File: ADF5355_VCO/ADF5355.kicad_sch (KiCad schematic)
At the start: 16 parts

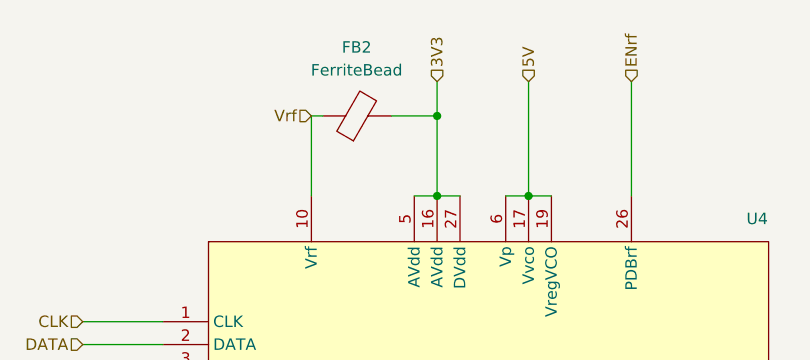
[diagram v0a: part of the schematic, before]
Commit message: Changed the power port
Changed all power ports to be global instead of them being hierarchical sheet pins
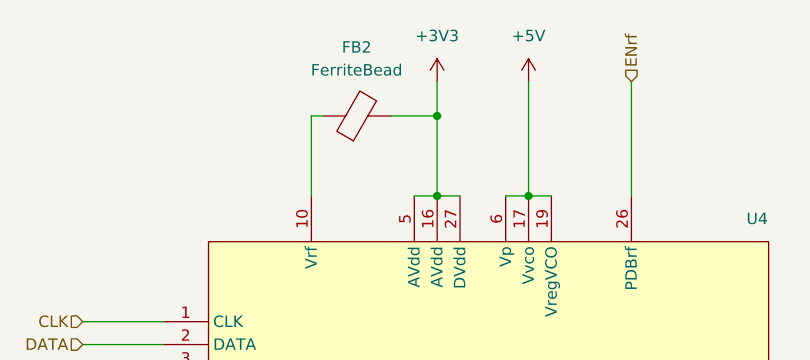
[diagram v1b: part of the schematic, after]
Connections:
- net Vrf: no longer FB2.1, U4.10 (Vrf)
- net 3V3 renamed +3V3
- net 5V renamed +5V
- new net: FB2.1, U4.10 (Vrf)
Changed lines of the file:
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@@
-    (effects (font (size 1.27 1.27)) (justify left))
-  )
-  (hierarchical_label "5V" (shape input) (at 146.05 43.18 90) (fields_autoplaced)
     (effects (font (size 1.27 1.27)) (justify left))
   )
@@
     (effects (font (size 1.27 1.27)) (justify right))
   )
-  (hierarchical_label "Vrf" (shape input) (at 121.92 46.99 180) (fields_autoplaced)
-    (effects (font (size 1.27 1.27)) (justify right))
-  )
   (hierarchical_label "Vrf" (shape input) (at 185.42 66.04 90) (fields_autoplaced)
     (effects (font (size 1.27 1.27)) (justify left))
@@
   )
   (hierarchical_label "RFoutB" (shape input) (at 203.2 100.33 0) (fields_autoplaced)
-    (effects (font (size 1.27 1.27)) (justify left))
-  )
-  (hierarchical_label "3V3" (shape input) (at 135.89 43.18 90) (fields_autoplaced)
     (effects (font (size 1.27 1.27)) (justify left))
   )
@@
     )
   )
+  (symbol (lib_id "power:+5V") (at 146.05 43.18 0) (unit 1)
+    (in_bom yes) (on_board yes) (dnp no) (fields_autoplaced)
+    (property "Reference" "#PWR043" (at 146.05 46.99 0)
+      (effects (font (size 1.27 1.27)) hide)
+    )
+    (property "Value" "+5V" (at 146.05 38.1 0)
+      (effects (font (size 1.27 1.27)))
+    )
+    (property "Footprint" "" (at 146.05 43.18 0)
+      (effects (font (size 1.27 1.27)) hide)
+    )
+    (property "Datasheet" "" (at 146.05 43.18 0)
+      (effects (font (size 1.27 1.27)) hide)
+    )
+    (pin "1")
+    (instances
+      (project "ADF5355_VCO"
+        (path "/29349b68-071c-451b-9b1e-10b5ef7e12a6/ea810e70-e3dc-4641-ad7c-8ecf7484ded2"
+          (reference "#PWR043") (unit 1)
+        )
+      )
+    )
+  )
   (symbol (lib_id "Device:R") (at 215.9 81.28 90) (unit 1)
     (in_bom yes) (on_board yes) (dnp no)
@@
         )
       )
+    )
+  )
+  (symbol (lib_id "power:+3V3") (at 135.89 43.18 0) (unit 1)
+    (in_bom yes) (on_board yes) (dnp no) (fields_autoplaced)
+    (property "Reference" "#PWR042" (at 135.89 46.99 0)
+      (effects (font (size 1.27 1.27)) hide)
+    )
+    (property "Value" "+3V3" (at 135.89 38.1 0)
+      (effects (font (size 1.27 1.27)))
+    )
+    (property "Footprint" "" (at 135.89 43.18 0)
+      (effects (font (size 1.27 1.27)) hide)
+    )
+    (property "Datasheet" "" (at 135.89 43.18 0)
+      (effects (font (size 1.27 1.27)) hide)
+    )
+    (pin "1")
+    (instances
+      (project "ADF5355_VCO"
+        (path "/29349b68-071c-451b-9b1e-10b5ef7e12a6/ea810e70-e3dc-4641-ad7c-8ecf7484ded2"
+          (reference "#PWR042") (unit 1)
+        )
+      )

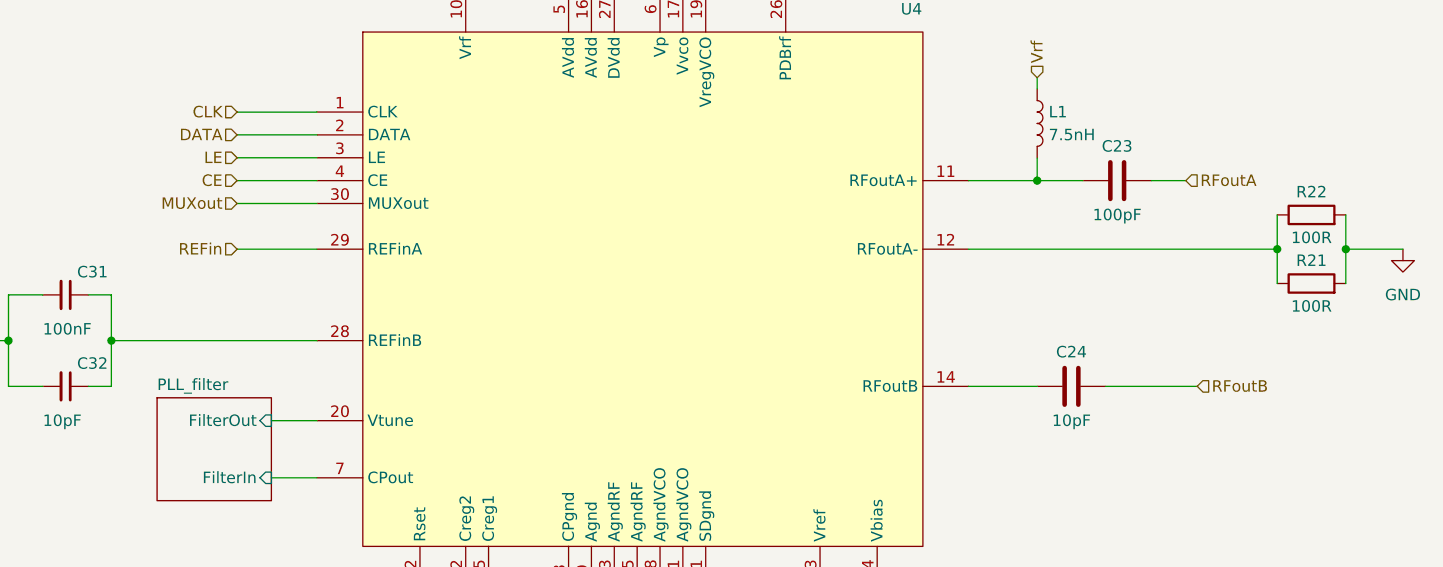
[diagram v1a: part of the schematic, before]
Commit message: Added RF connectors
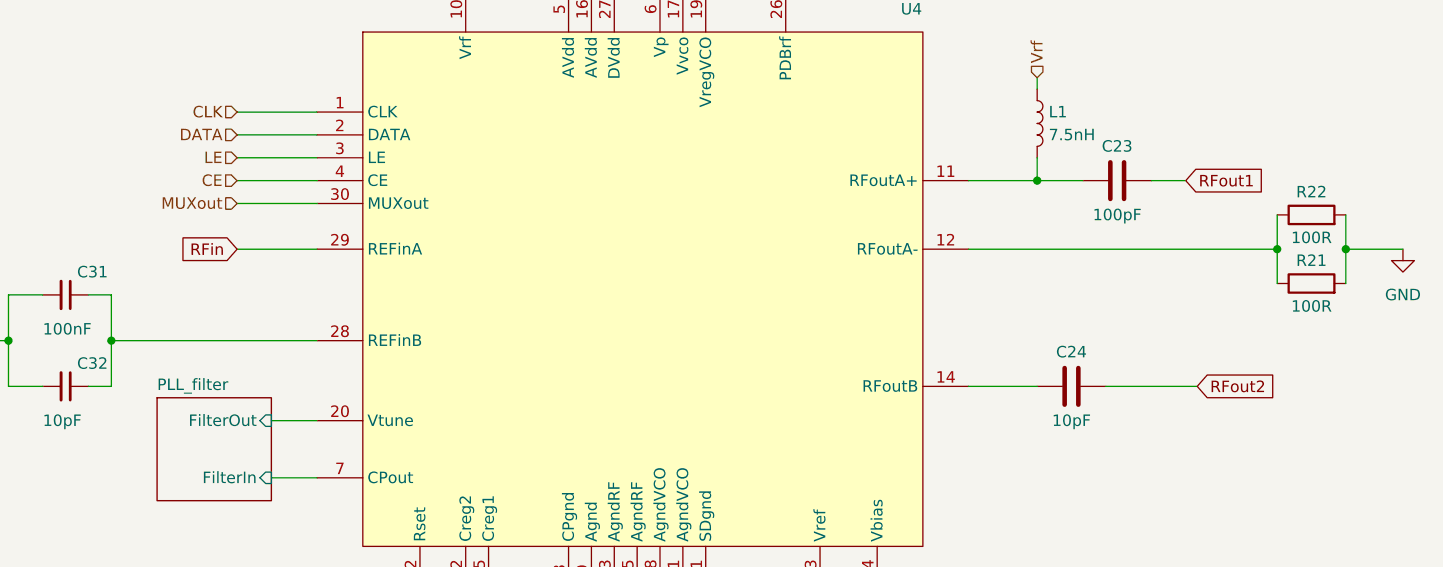
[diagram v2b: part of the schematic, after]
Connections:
- net REFin renamed RFin
- net RFoutA renamed RFout1
- net RFoutB renamed RFout2
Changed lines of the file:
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@@
     (stroke (width 0) (type default))
+  )
+  (global_label "RFin" (shape input) (at 96.52 85.09 180) (fields_autoplaced)
+    (effects (font (size 1.27 1.27)) (justify right))
+    (property "Intersheetrefs" "${INTERSHEET_REFS}" (at 90.156 85.09 0)
+      (effects (font (size 1.27 1.27)) (justify right) hide)
+    )
+  )
+  (global_label "RFout2" (shape input) (at 203.2 100.33 0) (fields_autoplaced)
+    (effects (font (size 1.27 1.27)) (justify left))
+    (property "Intersheetrefs" "${INTERSHEET_REFS}" (at 212.0434 100.33 0)
+      (effects (font (size 1.27 1.27)) (justify left) hide)
+    )
+  )
+  (global_label "RFout1" (shape input) (at 201.93 77.47 0) (fields_autoplaced)
+    (effects (font (size 1.27 1.27)) (justify left))
+    (property "Intersheetrefs" "${INTERSHEET_REFS}" (at 210.7734 77.47 0)
+      (effects (font (size 1.27 1.27)) (justify left) hide)
+    )
   )
   (hierarchical_label "DATA" (shape input) (at 96.52 72.39 180) (fields_autoplaced)
@@
     (effects (font (size 1.27 1.27)) (justify right))
   )
-  (hierarchical_label "REFin" (shape input) (at 96.52 85.09 180) (fields_autoplaced)
-    (effects (font (size 1.27 1.27)) (justify right))
-  )
-  (hierarchical_label "RFoutA" (shape input) (at 201.93 77.47 0) (fields_autoplaced)
-    (effects (font (size 1.27 1.27)) (justify left))
-  )
-  (hierarchical_label "RFoutB" (shape input) (at 203.2 100.33 0) (fields_autoplaced)
-    (effects (font (size 1.27 1.27)) (justify left))
-  )
   (symbol (lib_id "power:GND") (at 156.21 139.7 0) (unit 1)

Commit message: Added additional footprints and BOM
Added a bill of materials with most of the components.
Added footprints for more components
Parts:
- C25, C27, C29, C30, C31: footprint (none) -> Capacitor_SMD:C_0603_1608Metric_Pad1.08x0.95mm_HandSolder
- R21, R22, R23: footprint (none) -> Resistor_SMD:R_0603_1608Metric_Pad0.98x0.95mm_HandSolder
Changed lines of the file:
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@@
       (effects (font (size 1.27 1.27)) (justify left))
     )
-    (property "Footprint" "" (at 113.03 130.81 0)
+    (property "Footprint" "Resistor_SMD:R_0603_1608Metric_Pad0.98x0.95mm_HandSolder" (at 113.03 130.81 0)
       (effects (font (size 1.27 1.27)) hide)
     )
@@
       (effects (font (size 1.27 1.27)))
     )
-    (property "Footprint" "" (at 215.9 90.678 90)
+    (property "Footprint" "Resistor_SMD:R_0603_1608Metric_Pad0.98x0.95mm_HandSolder" (at 215.9 90.678 90)
       (effects (font (size 1.27 1.27)) hide)
     )
@@
       (effects (font (size 1.27 1.27)))
     )
-    (property "Footprint" "" (at 215.9 83.058 90)
+    (property "Footprint" "Resistor_SMD:R_0603_1608Metric_Pad0.98x0.95mm_HandSolder" (at 215.9 83.058 90)
       (effects (font (size 1.27 1.27)) hide)
     )
@@
       (effects (font (size 1.27 1.27)) (justify left))
     )
-    (property "Footprint" "" (at 119.38 133.35 0)
+    (property "Footprint" "Capacitor_SMD:C_0603_1608Metric_Pad1.08x0.95mm_HandSolder" (at 119.38 133.35 0)
       (effects (font (size 1.27 1.27)) hide)
     )
@@
       (effects (font (size 1.27 1.27)) (justify left))
     )
-    (property "Footprint" "" (at 171.45 133.35 0)
+    (property "Footprint" "Capacitor_SMD:C_0603_1608Metric_Pad1.08x0.95mm_HandSolder" (at 171.45 133.35 0)
       (effects (font (size 1.27 1.27)) hide)
     )
@@
       (effects (font (size 1.27 1.27)) (justify left))
     )
-    (property "Footprint" "" (at 129.54 133.35 0)
+    (property "Footprint" "Capacitor_SMD:C_0603_1608Metric_Pad1.08x0.95mm_HandSolder" (at 129.54 133.35 0)
       (effects (font (size 1.27 1.27)) hide)
     )
@@
       (effects (font (size 1.27 1.27)) (justify left))
     )
-    (property "Footprint" "" (at 151.13 133.35 0)
+    (property "Footprint" "Capacitor_SMD:C_0603_1608Metric_Pad1.08x0.95mm_HandSolder" (at 151.13 133.35 0)
       (effects (font (size 1.27 1.27)) hide)
     )
@@
       (effects (font (size 1.27 1.27)) (justify left))
     )
-    (property "Footprint" "" (at 77.47 90.17 0)
-      (effects (font (size 1.27 1.27)) hide)
-    )
+    (property "Footprint" "Capacitor_SMD:C_0603_1608Metric_Pad1.08x0.95mm_HandSolder" (at 77.47 90.17 0)
+      (effects (font (size 1.27 1.27)) hide)
+    )

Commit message: Added PLL filter
Added components for the PLL filter
 according to the components on evaluation board

Added specific components to BOM
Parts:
- C26, C28, C32: footprint (none) -> Capacitor_SMD:C_0603_1608Metric_Pad1.08x0.95mm_HandSolder
- U4: footprint (none) -> ADF5355_footprint_lib:162K-CC_BC-3LP
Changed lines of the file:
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@@
       (effects (font (size 1.27 1.27)))
     )
-    (property "Footprint" "" (at 138.43 69.85 0)
+    (property "Footprint" "ADF5355_footprint_lib:162K-CC_BC-3LP" (at 138.43 69.85 0)
       (effects (font (size 1.27 1.27)) hide)
     )
@@
       (effects (font (size 1.27 1.27)) (justify left))
     )
-    (property "Footprint" "" (at 77.47 100.33 0)
+    (property "Footprint" "Capacitor_SMD:C_0603_1608Metric_Pad1.08x0.95mm_HandSolder" (at 77.47 100.33 0)
       (effects (font (size 1.27 1.27)) hide)
     )
@@
       (effects (font (size 1.27 1.27)) (justify left))
     )
-    (property "Footprint" "" (at 181.61 133.35 0)
+    (property "Footprint" "Capacitor_SMD:C_0603_1608Metric_Pad1.08x0.95mm_HandSolder" (at 181.61 133.35 0)
       (effects (font (size 1.27 1.27)) hide)
     )
@@
       (effects (font (size 1.27 1.27)) (justify left))
     )
-    (property "Footprint" "" (at 161.29 133.35 0)
-      (effects (font (size 1.27 1.27)) hide)
-    )
+    (property "Footprint" "Capacitor_SMD:C_0603_1608Metric_Pad1.08x0.95mm_HandSolder" (at 161.29 133.35 0)
+      (effects (font (size 1.27 1.27)) hide)
+    )

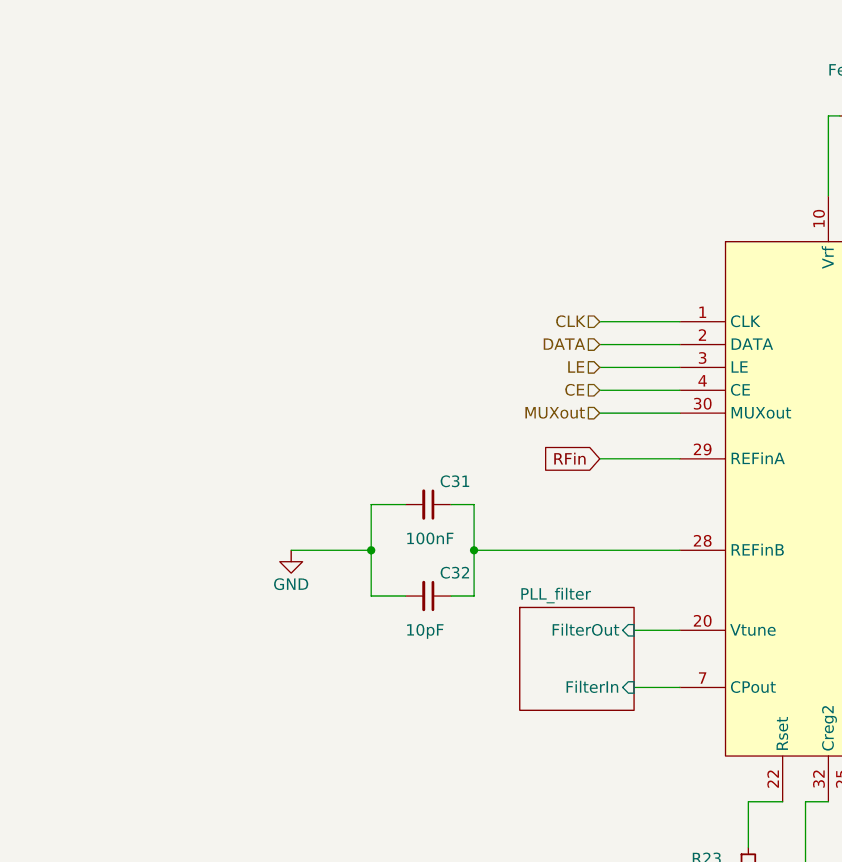
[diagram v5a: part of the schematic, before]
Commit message: Added TCXO and remaining footprints
Added remaining footprints
    NX3225GD
    710X toggle switch
    SMT button

Added ClearClock AX3 TCXO symbol and footprint

Added TCXO schematic with 3 options:
    LVPECL, LVDS and HCSL
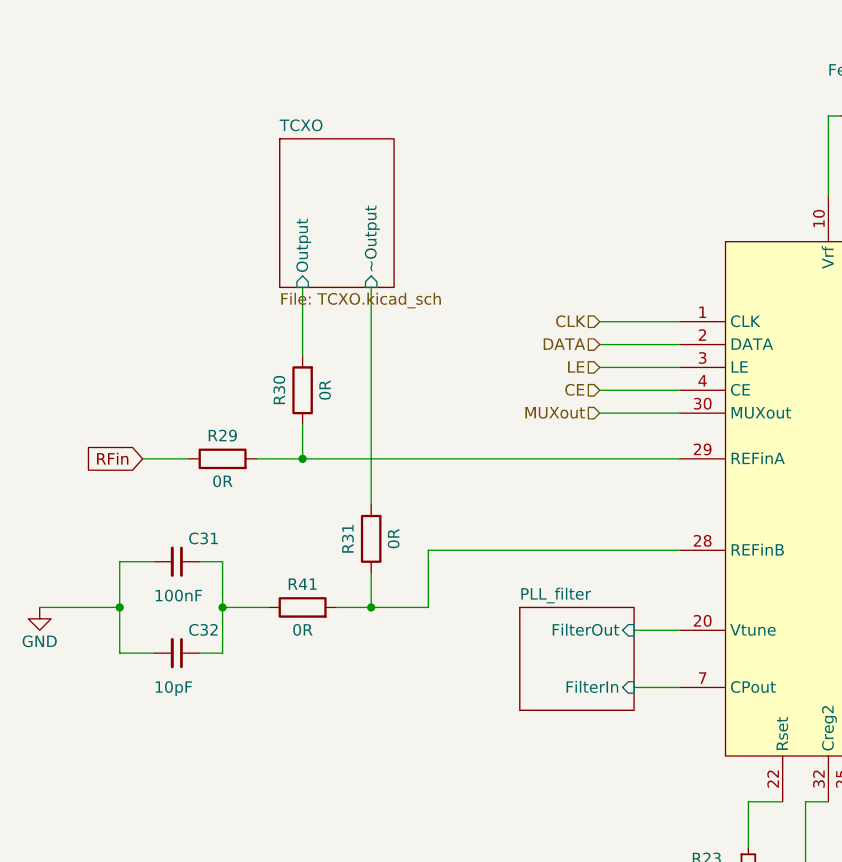
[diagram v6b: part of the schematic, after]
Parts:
- added R29, R30, R31, R41: 0R, symbol Device:R
- C23, C24: footprint (none) -> Capacitor_SMD:C_0201_0603Metric_Pad0.64x0.40mm_HandSolder
- FB2: footprint (none) -> Resistor_SMD:R_0603_1608Metric_Pad0.98x0.95mm_HandSolder
- L1: footprint (none) -> Capacitor_SMD:C_0402_1005Metric_Pad0.74x0.62mm_HandSolder
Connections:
- net RFin: now also R29.1; no longer U4.29 (REFinA)
- net at C31.1, C32.1: now also R41.1; no longer U4.28 (REFinB)
- new net: R31.1, R41.2, U4.28 (REFinB)
- new net: R29.2, R30.1, U4.29 (REFinA)
- new net TCXO/Output: R30.2
- new net TCXO/~Output: R31.2
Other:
- added sheet TCXO (TCXO.kicad_sch)
- moved on the sheet: C31, C32
